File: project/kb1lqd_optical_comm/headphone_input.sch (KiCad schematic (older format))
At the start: 0 parts

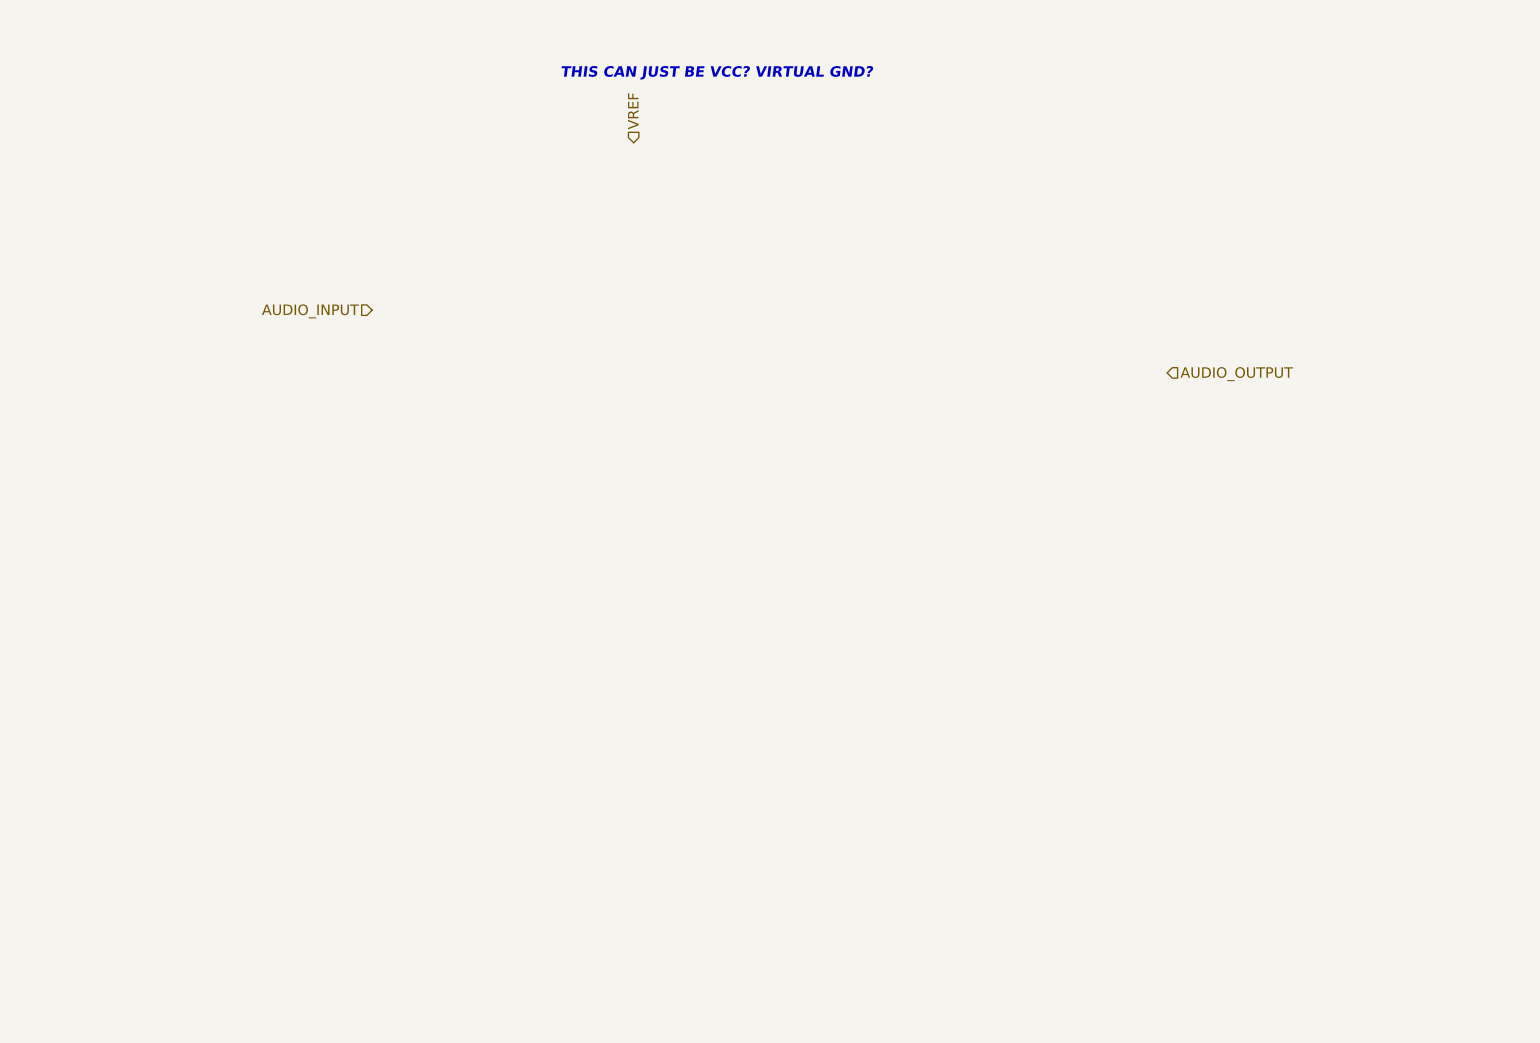
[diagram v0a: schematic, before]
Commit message: Updated with better values and text.
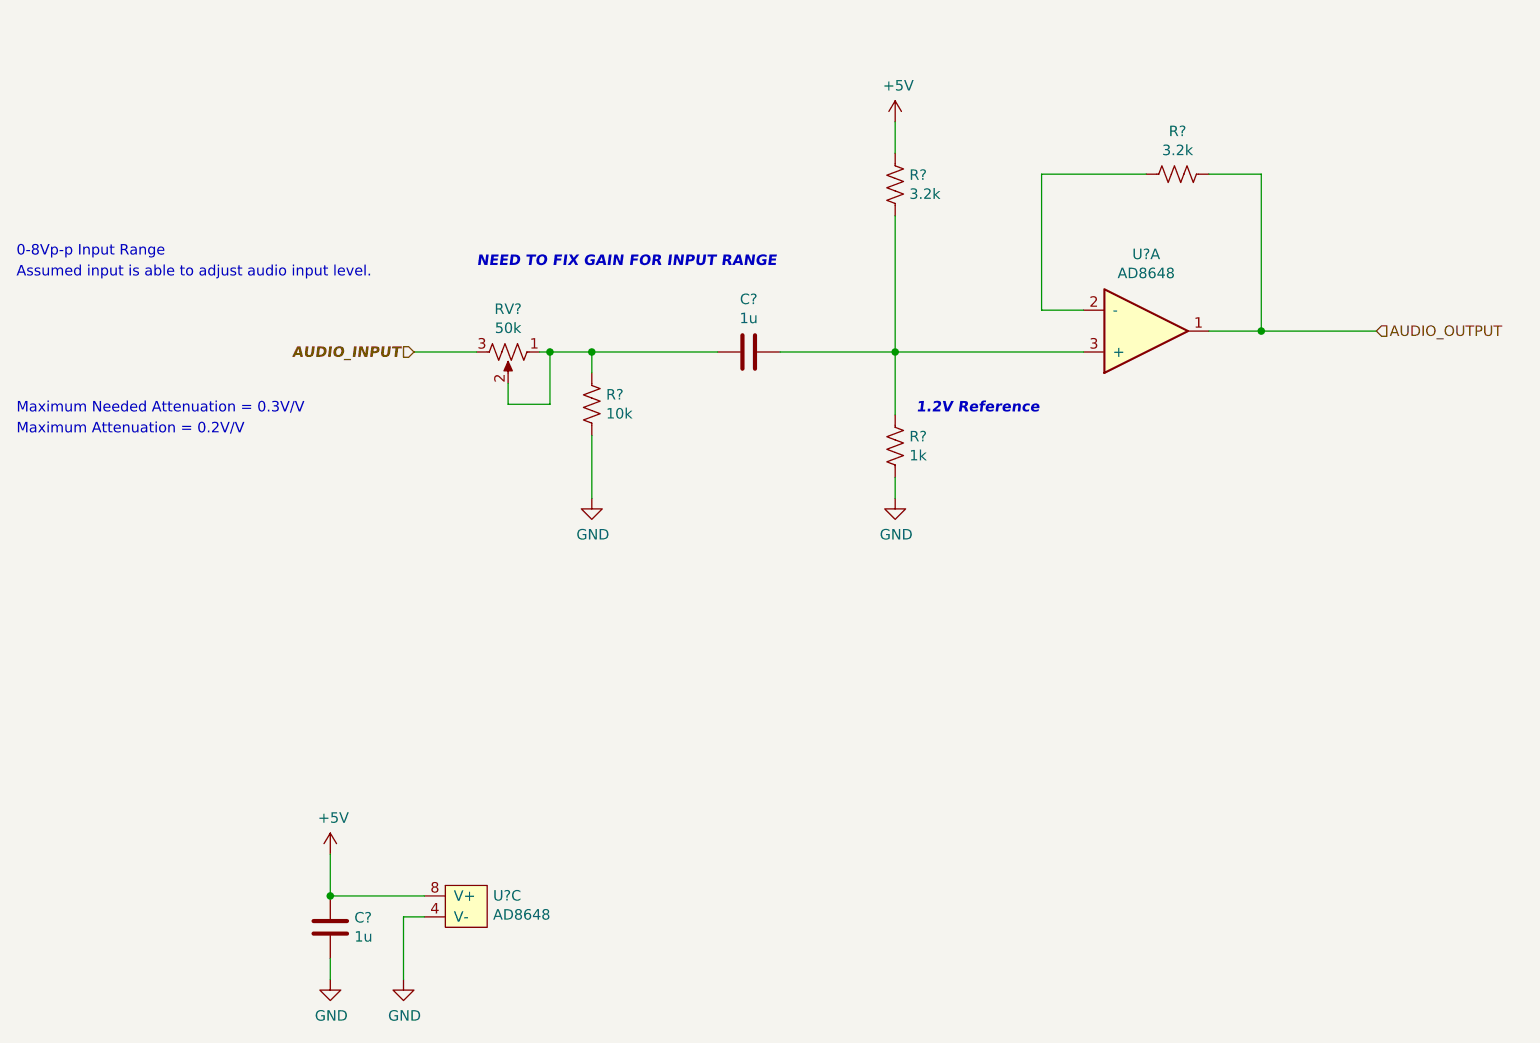
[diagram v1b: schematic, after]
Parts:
- added C? (x2): 1u, symbol Device:C
- added R?: 10k, symbol Device:R_US
- added R? (x2): 3.2k, symbol Device:R_US
- added R?: 1k, symbol Device:R_US
- added RV?: 50k, symbol Device:R_POT_US
- added U? (x2): AD8648, symbol kb1lqd_optical_comm:AD8648
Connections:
- net AUDIO_INPUT: now also RV?.3
- net AUDIO_OUTPUT: now also R?.1, U?.1
- new net: R?.2, U?.2 (-)
- new net: C?.1, R?.1, R?.2, U?.3 (+)
- new net: C?.2, R?.1, RV?.1, RV?.2
- new net +5V: C?.2, R?.1, U?.8 (V+)
- new net GND: C?.1, R?.2, R?.2, U?.4 (V-)
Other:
- note added: "0-8Vp-p Input Range"
- note added: "1.2V Reference"
- note added: "Assumed input is able to adjust audio input level."
- note added: "Maximum Attenuation = 0.2V/V"
- note added: "Maximum Needed Attenuation = 0.3V/V\n"
- note added: "NEED TO FIX GAIN FOR INPUT RANGE"
- note removed: "THIS CAN JUST BE VCC? VIRTUAL GND?"

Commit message: Adding updates.
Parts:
- added R?: 0, symbol Device:R_US
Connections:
- net AUDIO_OUTPUT: now also R?.1; no longer U?.1
- new net: R?.2, U?.1
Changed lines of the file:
@@
 	5150 3500 6050 3500
 Wire Wire Line
-	6650 3400 6900 3400
+	6650 3400 6800 3400
 Wire Wire Line
 	5850 2650 5850 3300
@@
 NEED TO FIX GAIN FOR INPUT RANGE
 Wire Wire Line
-	6900 2650 6900 3400
+	7300 2650 7300 3400
 Wire Wire Line
-	6900 2650 6650 2650
-Connection ~ 6900 3400
+	7300 2650 6650 2650
+Connection ~ 7300 3400
 Wire Wire Line
-	6900 3400 7450 3400
+	7300 3400 7450 3400
 Text Notes 950  3050 0    50   ~ 0
 0-8Vp-p Input Range
@@
 Text Notes 950  3900 0    50   ~ 0
 Maximum Attenuation = 0.2V/V
+$Comp
+L Device:R_US R?
+U 1 1 5F6E86E4
+P 6950 3400
+AR Path="/5F64B8C0/5F6E86E4" Ref="R?"  Part="1"
+AR Path="/5F64BA55/5F6E86E4" Ref="R?"  Part="1"
+F 0 "R?" V 6745 3400 50  0000 C CNN
+F 1 "0" V 6836 3400 50  0000 C CNN
+F 2 "" V 6990 3390 50  0001 C CNN
+F 3 "~" H 6950 3400 50  0001 C CNN
+	1    6950 3400
+	0    1    1    0
+$EndComp
+Wire Wire Line
+	7100 3400 7300 3400
 $EndSCHEMATC

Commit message: Adding updates for 9/21/2020
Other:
- note removed: "NEED TO FIX GAIN FOR INPUT RANGE"
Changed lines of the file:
@@
 Text Notes 5250 3800 0    50   Italic 10
 1.2V Reference
-Text Notes 3150 3100 0    50   Italic 10
-NEED TO FIX GAIN FOR INPUT RANGE
 Wire Wire Line
 	7300 2650 7300 3400

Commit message: Schematic essentially done.
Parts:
- added C? (x2): DNP, symbol Device:C
- gave numbers to parts that had none: 9
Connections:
- net AUDIO_OUTPUT: now also C?.1
- net GND: now also C?.2
- net at R16.2, U1.2 (-): now also C?.2
- net at C3.1, R14.2, R15.1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: now also C?.1
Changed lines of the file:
@@
 $Descr A4 11693 8268
 encoding utf-8
-Sheet 3 5
+Sheet 3 6
 Title ""
 Date ""
@@
 AUDIO_OUTPUT
 $Comp
-L kb1lqd_optical_comm:AD8648 U?
+L kb1lqd_optical_comm:AD8648 U1
 U 1 1 5F6A682E
 P 5700 3000
-F 0 "U?" H 6350 3033 50  0000 C CNN
+F 0 "U1" H 6350 3033 50  0000 C CNN
 F 1 "AD8648" H 6350 3124 50  0000 C CNN
 F 2 "" H 5700 3000 50  0001 C CNN
@@
 $EndComp
 $Comp
-L kb1lqd_optical_comm:AD8648 U?
+L kb1lqd_optical_comm:AD8648 U1
 U 3 1 5F6A6CAB
 P 2550 6500
-F 0 "U?" H 3228 6901 50  0000 L CNN
+F 0 "U1" H 3228 6901 50  0000 L CNN
 F 1 "AD8648" H 3228 6810 50  0000 L CNN
 F 2 "" H 2550 6500 50  0001 C CNN
@@
 P 3700 3750
 AR Path="/5F64B8C0/5F6AD538" Ref="R?"  Part="1"
-AR Path="/5F64BA55/5F6AD538" Ref="R?"  Part="1"
-F 0 "R?" H 3768 3796 50  0000 L CNN
+AR Path="/5F64BA55/5F6AD538" Ref="R13"  Part="1"
+F 0 "R13" H 3768 3796 50  0000 L CNN
 F 1 "10k" H 3768 3705 50  0000 L CNN
 F 2 "" V 3740 3740 50  0001 C CNN
@@
 P 5150 2700
 AR Path="/5F64B8C0/5F6AD53E" Ref="R?"  Part="1"
-AR Path="/5F64BA55/5F6AD53E" Ref="R?"  Part="1"
-F 0 "R?" H 5218 2746 50  0000 L CNN
+AR Path="/5F64BA55/5F6AD53E" Ref="R14"  Part="1"
+F 0 "R14" H 5218 2746 50  0000 L CNN
 F 1 "3.2k" H 5218 2655 50  0000 L CNN
 F 2 "" V 5190 2690 50  0001 C CNN
@@
 P 5150 3950
 AR Path="/5F64B8C0/5F6AD54B" Ref="R?"  Part="1"
-AR Path="/5F64BA55/5F6AD54B" Ref="R?"  Part="1"
-F 0 "R?" H 5218 3996 50  0000 L CNN
+AR Path="/5F64BA55/5F6AD54B" Ref="R15"  Part="1"
+F 0 "R15" H 5218 3996 50  0000 L CNN
 F 1 "1k" H 5218 3905 50  0000 L CNN
 F 2 "" V 5190 3940 50  0001 C CNN
@@
 P 3700 4200
 AR Path="/5F64B8C0/5F6AD551" Ref="#PWR?"  Part="1"
-AR Path="/5F64BA55/5F6AD551" Ref="#PWR?"  Part="1"
-F 0 "#PWR?" H 3700 3950 50  0001 C CNN
+AR Path="/5F64BA55/5F6AD551" Ref="#PWR016"  Part="1"
+F 0 "#PWR016" H 3700 3950 50  0001 C CNN
 F 1 "GND" H 3705 4027 50  0000 C CNN
 F 2 "" H 3700 4200 50  0001 C CNN
@@
 P 5150 2400
 AR Path="/5F64B8C0/5F6AD557" Ref="#PWR?"  Part="1"
-AR Path="/5F64BA55/5F6AD557" Ref="#PWR?"  Part="1"
-F 0 "#PWR?" H 5150 2250 50  0001 C CNN
+AR Path="/5F64BA55/5F6AD557" Ref="#PWR017"  Part="1"
+F 0 "#PWR017" H 5150 2250 50  0001 C CNN
 F 1 "+5V" H 5165 2573 50  0000 C CNN
 F 2 "" H 5150 2400 50  0001 C CNN
@@
 Connection ~ 5150 3500
 Wire Wire Line
-	5150 3500 5150 3800
+	5150 3500 5150 3700
 Wire Wire Line
 	5150 3500 6050 3500
@@
 P 6500 2650
 AR Path="/5F64B8C0/5F6AD566" Ref="R?"  Part="1"
-AR Path="/5F64BA55/5F6AD566" Ref="R?"  Part="1"
-F 0 "R?" V 6295 2650 50  0000 C CNN
+AR Path="/5F64BA55/5F6AD566" Ref="R16"  Part="1"
+F 0 "R16" V 6295 2650 50  0000 C CNN
 F 1 "3.2k" V 6386 2650 50  0000 C CNN
 F 2 "" V 6540 2640 50  0001 C CNN
@@
 P 5150 4200
 AR Path="/5F64B8C0/5F6AD56D" Ref="#PWR?"  Part="1"
-AR Path="/5F64BA55/5F6AD56D" Ref="#PWR?"  Part="1"
-F 0 "#PWR?" H 5150 3950 50  0001 C CNN
+AR Path="/5F64BA55/5F6AD56D" Ref="#PWR018"  Part="1"
+F 0 "#PWR018" H 5150 3950 50  0001 C CNN
 F 1 "GND" H 5155 4027 50  0000 C CNN
 F 2 "" H 5150 4200 50  0001 C CNN
@@
 P 3300 3500
 AR Path="/5F64AFB2/5F6BCCAE" Ref="RV?"  Part="1"
-AR Path="/5F64BA55/5F6BCCAE" Ref="RV?"  Part="1"
-F 0 "RV?" V 3095 3500 50  0000 C CNN
+AR Path="/5F64BA55/5F6BCCAE" Ref="RV1"  Part="1"
+F 0 "RV1" V 3095 3500 50  0000 C CNN
 F 1 "50k" V 3186 3500 50  0000 C CNN
 F 2 "" H 3300 3500 50  0001 C CNN
@@
 P 2450 6250
 AR Path="/5F64AFB2/5F6CB199" Ref="C?"  Part="1"
-AR Path="/5F64BA55/5F6CB199" Ref="C?"  Part="1"
-F 0 "C?" H 2335 6204 50  0000 R CNN
+AR Path="/5F64BA55/5F6CB199" Ref="C2"  Part="1"
+F 0 "C2" H 2335 6204 50  0000 R CNN
 F 1 "1u" H 2335 6295 50  0000 R CNN
 F 2 "" H 2488 6100 50  0001 C CNN
@@
 P 2800 6500
 AR Path="/5F64AFB2/5F6CB19F" Ref="#PWR?"  Part="1"
-AR Path="/5F64BA55/5F6CB19F" Ref="#PWR?"  Part="1"
-F 0 "#PWR?" H 2800 6250 50  0001 C CNN
+AR Path="/5F64BA55/5F6CB19F" Ref="#PWR015"  Part="1"
+F 0 "#PWR015" H 2800 6250 50  0001 C CNN
 F 1 "GND" H 2805 6327 50  0000 C CNN
 F 2 "" H 2800 6500 50  0001 C CNN
@@
 P 2450 5900
 AR Path="/5F64AFB2/5F6CB1A5" Ref="#PWR?"  Part="1"
-AR Path="/5F64BA55/5F6CB1A5" Ref="#PWR?"  Part="1"
-F 0 "#PWR?" H 2450 5750 50  0001 C CNN
+AR Path="/5F64BA55/5F6CB1A5" Ref="#PWR013"  Part="1"
+F 0 "#PWR013" H 2450 5750 50  0001 C CNN
 F 1 "+5V" H 2465 6073 50  0000 C CNN
 F 2 "" H 2450 5900 50  0001 C CNN
@@
 P 2450 6500
 AR Path="/5F64AFB2/5F6CB1AE" Ref="#PWR?"  Part="1"
-AR Path="/5F64BA55/5F6CB1AE" Ref="#PWR?"  Part="1"
-F 0 "#PWR?" H 2450 6250 50  0001 C CNN
+AR Path="/5F64BA55/5F6CB1AE" Ref="#PWR014"  Part="1"
+F 0 "#PWR014" H 2450 6250 50  0001 C CNN
 F 1 "GND" H 2455 6327 50  0000 C CNN
 F 2 "" H 2450 6500 50  0001 C CNN
@@
 Connection ~ 2450 6100
 $Comp
-L Device:C C?
+L Device:C C3
 U 1 1 5F6CE36E
 P 4450 3500
-F 0 "C?" V 4198 3500 50  0000 C CNN
+F 0 "C3" V 4198 3500 50  0000 C CNN
 F 1 "1u" V 4289 3500 50  0000 C CNN
 F 2 "" H 4488 3350 50  0001 C CNN
@@
 P 6950 3400
 AR Path="/5F64B8C0/5F6E86E4" Ref="R?"  Part="1"
-AR Path="/5F64BA55/5F6E86E4" Ref="R?"  Part="1"
-F 0 "R?" V 6745 3400 50  0000 C CNN
+AR Path="/5F64BA55/5F6E86E4" Ref="R17"  Part="1"
+F 0 "R17" V 6745 3400 50  0000 C CNN
 F 1 "0" V 6836 3400 50  0000 C CNN
 F 2 "" V 6990 3390 50  0001 C CNN
@@
 Wire Wire Line
 	7100 3400 7300 3400
+$Comp
+L Device:C C?
+U 1 1 5FE6D5BB
+P 6500 2200
+F 0 "C?" V 6248 2200 50  0000 C CNN
+F 1 "DNP" V 6339 2200 50  0000 C CNN
+F 2 "" H 6538 2050 50  0001 C CNN
+F 3 "~" H 6500 2200 50  0001 C CNN
+	1    6500 2200
+	0    1    1    0
+$EndComp
+Wire Wire Line
+	6350 2200 5850 2200
+Wire Wire Line
+	5850 2200 5850 2650
+Connection ~ 5850 2650
+Wire Wire Line
+	6650 2200 7300 2200
+Wire Wire Line
+	7300 2200 7300 2650
+Connection ~ 7300 2650
+$Comp
+L Device:C C?
+U 1 1 5FE76C59
+P 4750 3950
+F 0 "C?" V 4498 3950 50  0000 C CNN
+F 1 "DNP" V 4589 3950 50  0000 C CNN
+F 2 "" H 4788 3800 50  0001 C CNN
+F 3 "~" H 4750 3950 50  0001 C CNN
+	1    4750 3950
+	1    0    0    -1
+$EndComp
+Wire Wire Line
+	4750 3800 4750 3700
+Wire Wire Line
+	4750 3700 5150 3700
+Connection ~ 5150 3700
+Wire Wire Line
+	5150 3700 5150 3800
+Wire Wire Line
+	4750 4100 4750 4200
+$Comp
+L power:GND #PWR?
+U 1 1 5FE7838A
+P 4750 4200
+AR Path="/5F64B8C0/5FE7838A" Ref="#PWR?"  Part="1"
+AR Path="/5F64BA55/5FE7838A" Ref="#PWR?"  Part="1"
+F 0 "#PWR?" H 4750 3950 50  0001 C CNN
+F 1 "GND" H 4755 4027 50  0000 C CNN
+F 2 "" H 4750 4200 50  0001 C CNN
+F 3 "" H 4750 4200 50  0001 C CNN
+	1    4750 4200
+	1    0    0    -1
+$EndComp
 $EndSCHEMATC

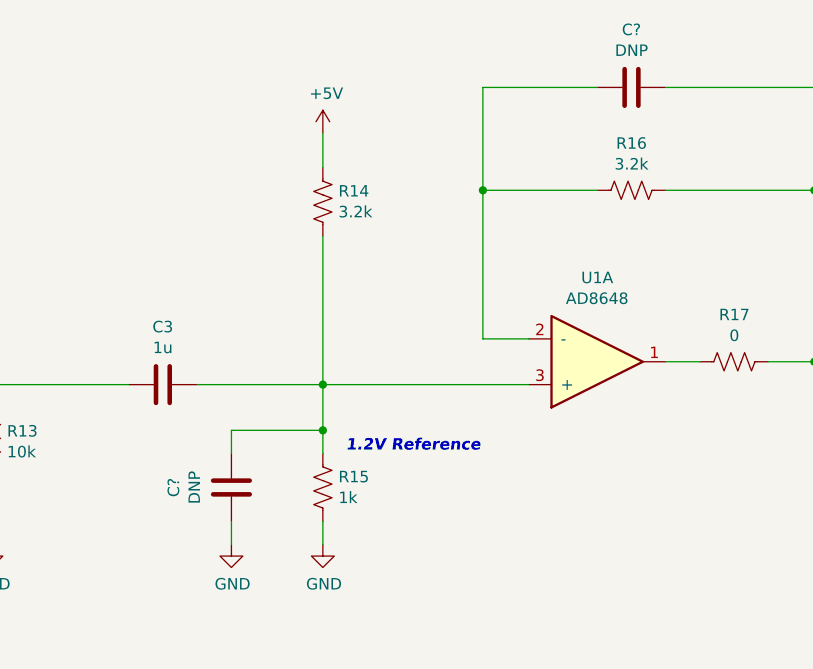
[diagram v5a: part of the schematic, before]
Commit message: Fixing ERC errors.
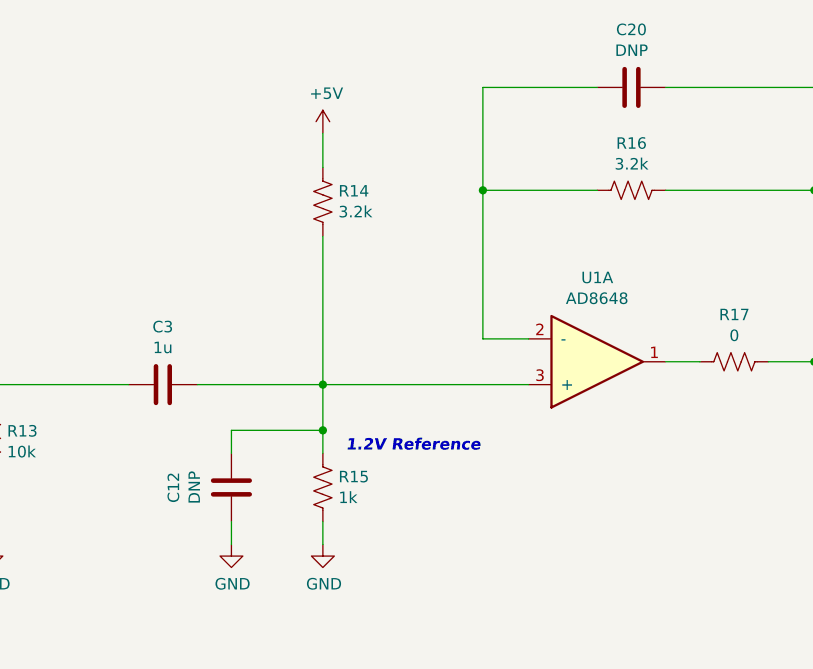
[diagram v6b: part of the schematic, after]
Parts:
- gave numbers to parts that had none: 2
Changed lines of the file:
@@
 	7100 3400 7300 3400
 $Comp
-L Device:C C?
+L Device:C C20
 U 1 1 5FE6D5BB
 P 6500 2200
-F 0 "C?" V 6248 2200 50  0000 C CNN
+F 0 "C20" V 6248 2200 50  0000 C CNN
 F 1 "DNP" V 6339 2200 50  0000 C CNN
 F 2 "" H 6538 2050 50  0001 C CNN
@@
 Connection ~ 7300 2650
 $Comp
-L Device:C C?
+L Device:C C12
 U 1 1 5FE76C59
 P 4750 3950
-F 0 "C?" V 4498 3950 50  0000 C CNN
+F 0 "C12" V 4498 3950 50  0000 C CNN
 F 1 "DNP" V 4589 3950 50  0000 C CNN
 F 2 "" H 4788 3800 50  0001 C CNN
@@
 P 4750 4200
 AR Path="/5F64B8C0/5FE7838A" Ref="#PWR?"  Part="1"
-AR Path="/5F64BA55/5FE7838A" Ref="#PWR?"  Part="1"
-F 0 "#PWR?" H 4750 3950 50  0001 C CNN
+AR Path="/5F64BA55/5FE7838A" Ref="#PWR0103"  Part="1"
+F 0 "#PWR0103" H 4750 3950 50  0001 C CNN
 F 1 "GND" H 4755 4027 50  0000 C CNN
 F 2 "" H 4750 4200 50  0001 C CNN

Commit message: Updated with all footprints
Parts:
- C12: footprint (none) -> Capacitor_SMD:C_0805_2012Metric
- C2, C3: footprint (none) -> Capacitor_SMD:C_1206_3216Metric
- C20: footprint (none) -> Capacitor_SMD:C_0201_0603Metric
- R13, R14, R15, R16, R17: footprint (none) -> Resistor_SMD:R_0603_1608Metric
- RV1: footprint (none) -> Connector_Molex:Molex_KK-254_AE-6410-04A_1x04_P2.54mm_Vertical
- U1: footprint (none) -> Package_SO:TSSOP-14_4.4x5mm_P0.65mm
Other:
- note added: "PTV09A-4025F-B503"
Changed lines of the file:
@@
 F 0 "U1" H 6350 3033 50  0000 C CNN
 F 1 "AD8648" H 6350 3124 50  0000 C CNN
-F 2 "" H 5700 3000 50  0001 C CNN
+F 2 "Package_SO:TSSOP-14_4.4x5mm_P0.65mm" H 5700 3000 50  0001 C CNN
 F 3 "" H 5700 3000 50  0001 C CNN
 	1    5700 3000
@@
 F 0 "U1" H 3228 6901 50  0000 L CNN
 F 1 "AD8648" H 3228 6810 50  0000 L CNN
-F 2 "" H 2550 6500 50  0001 C CNN
+F 2 "Package_SO:TSSOP-14_4.4x5mm_P0.65mm" H 2550 6500 50  0001 C CNN
 F 3 "" H 2550 6500 50  0001 C CNN
 	3    2550 6500
@@
 F 0 "R13" H 3768 3796 50  0000 L CNN
 F 1 "10k" H 3768 3705 50  0000 L CNN
-F 2 "" V 3740 3740 50  0001 C CNN
+F 2 "Resistor_SMD:R_0603_1608Metric" V 3740 3740 50  0001 C CNN
 F 3 "~" H 3700 3750 50  0001 C CNN
 	1    3700 3750
@@
 F 0 "R14" H 5218 2746 50  0000 L CNN
 F 1 "3.2k" H 5218 2655 50  0000 L CNN
-F 2 "" V 5190 2690 50  0001 C CNN
+F 2 "Resistor_SMD:R_0603_1608Metric" V 5190 2690 50  0001 C CNN
 F 3 "~" H 5150 2700 50  0001 C CNN
 	1    5150 2700
@@
 F 0 "R15" H 5218 3996 50  0000 L CNN
 F 1 "1k" H 5218 3905 50  0000 L CNN
-F 2 "" V 5190 3940 50  0001 C CNN
+F 2 "Resistor_SMD:R_0603_1608Metric" V 5190 3940 50  0001 C CNN
 F 3 "~" H 5150 3950 50  0001 C CNN
 	1    5150 3950
@@
 F 0 "R16" V 6295 2650 50  0000 C CNN
 F 1 "3.2k" V 6386 2650 50  0000 C CNN
-F 2 "" V 6540 2640 50  0001 C CNN
+F 2 "Resistor_SMD:R_0603_1608Metric" V 6540 2640 50  0001 C CNN
 F 3 "~" H 6500 2650 50  0001 C CNN
 	1    6500 2650
@@
 F 0 "RV1" V 3095 3500 50  0000 C CNN
 F 1 "50k" V 3186 3500 50  0000 C CNN
-F 2 "" H 3300 3500 50  0001 C CNN
+F 2 "Connector_Molex:Molex_KK-254_AE-6410-04A_1x04_P2.54mm_Vertical" H 3300 3500 50  0001 C CNN
 F 3 "~" H 3300 3500 50  0001 C CNN
 	1    3300 3500
@@
 F 0 "C2" H 2335 6204 50  0000 R CNN
 F 1 "1u" H 2335 6295 50  0000 R CNN
-F 2 "" H 2488 6100 50  0001 C CNN
+F 2 "Capacitor_SMD:C_1206_3216Metric" H 2488 6100 50  0001 C CNN
 F 3 "~" H 2450 6250 50  0001 C CNN
 	1    2450 6250
@@
 F 0 "C3" V 4198 3500 50  0000 C CNN
 F 1 "1u" V 4289 3500 50  0000 C CNN
-F 2 "" H 4488 3350 50  0001 C CNN
+F 2 "Capacitor_SMD:C_1206_3216Metric" H 4488 3350 50  0001 C CNN
 F 3 "~" H 4450 3500 50  0001 C CNN
 	1    4450 3500
@@
 F 0 "R17" V 6745 3400 50  0000 C CNN
 F 1 "0" V 6836 3400 50  0000 C CNN
-F 2 "" V 6990 3390 50  0001 C CNN
+F 2 "Resistor_SMD:R_0603_1608Metric" V 6990 3390 50  0001 C CNN
 F 3 "~" H 6950 3400 50  0001 C CNN
 	1    6950 3400
@@
 F 0 "C20" V 6248 2200 50  0000 C CNN
 F 1 "DNP" V 6339 2200 50  0000 C CNN
-F 2 "" H 6538 2050 50  0001 C CNN
+F 2 "Capacitor_SMD:C_0201_0603Metric" H 6538 2050 50  0001 C CNN
 F 3 "~" H 6500 2200 50  0001 C CNN
 	1    6500 2200
@@
 F 0 "C12" V 4498 3950 50  0000 C CNN
 F 1 "DNP" V 4589 3950 50  0000 C CNN
-F 2 "" H 4788 3800 50  0001 C CNN
+F 2 "Capacitor_SMD:C_0805_2012Metric" H 4788 3800 50  0001 C CNN
 F 3 "~" H 4750 3950 50  0001 C CNN
 	1    4750 3950
@@
 	1    0    0    -1
 $EndComp
+Text Notes 3100 3250 0    50   ~ 0
+PTV09A-4025F-B503
 $EndSCHEMATC

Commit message: Initial placement mostly done. Outlined PCB.
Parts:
- C20: footprint Capacitor_SMD:C_0201_0603Metric -> Capacitor_SMD:C_0805_2012Metric
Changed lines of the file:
@@
 F 0 "C20" V 6248 2200 50  0000 C CNN
 F 1 "DNP" V 6339 2200 50  0000 C CNN
-F 2 "Capacitor_SMD:C_0201_0603Metric" H 6538 2050 50  0001 C CNN
+F 2 "Capacitor_SMD:C_0805_2012Metric" H 6538 2050 50  0001 C CNN
 F 3 "~" H 6500 2200 50  0001 C CNN
 	1    6500 2200
